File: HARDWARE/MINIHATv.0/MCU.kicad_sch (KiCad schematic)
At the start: 0 parts

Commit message: Merge branch 'main' into display-basic-implementation
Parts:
- added U2: STM32H747IGTx, Package_QFP:LQFP-176_24x24mm_P0.5mm, symbol MCU_ST_STM32H7:STM32H747IGTx
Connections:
- new net: U2.100 (VSS), U2.112 (VSS), U2.119 (VSS), U2.12 (VSS), U2.134 (VSS), U2.137 (VSS), U2.151 (VSS), U2.159 (VSS), U2.173 (VSS), U2.24 (VSS), U2.45 (VSS), U2.47 (VSS), U2.6 (VSS), U2.64 (VSS), U2.70 (VSS), U2.81 (VSS), U2.83 (VSS), U2.93 (VSS)
- new net: U2.105 (VSSDSI), U2.109 (VSSDSI)

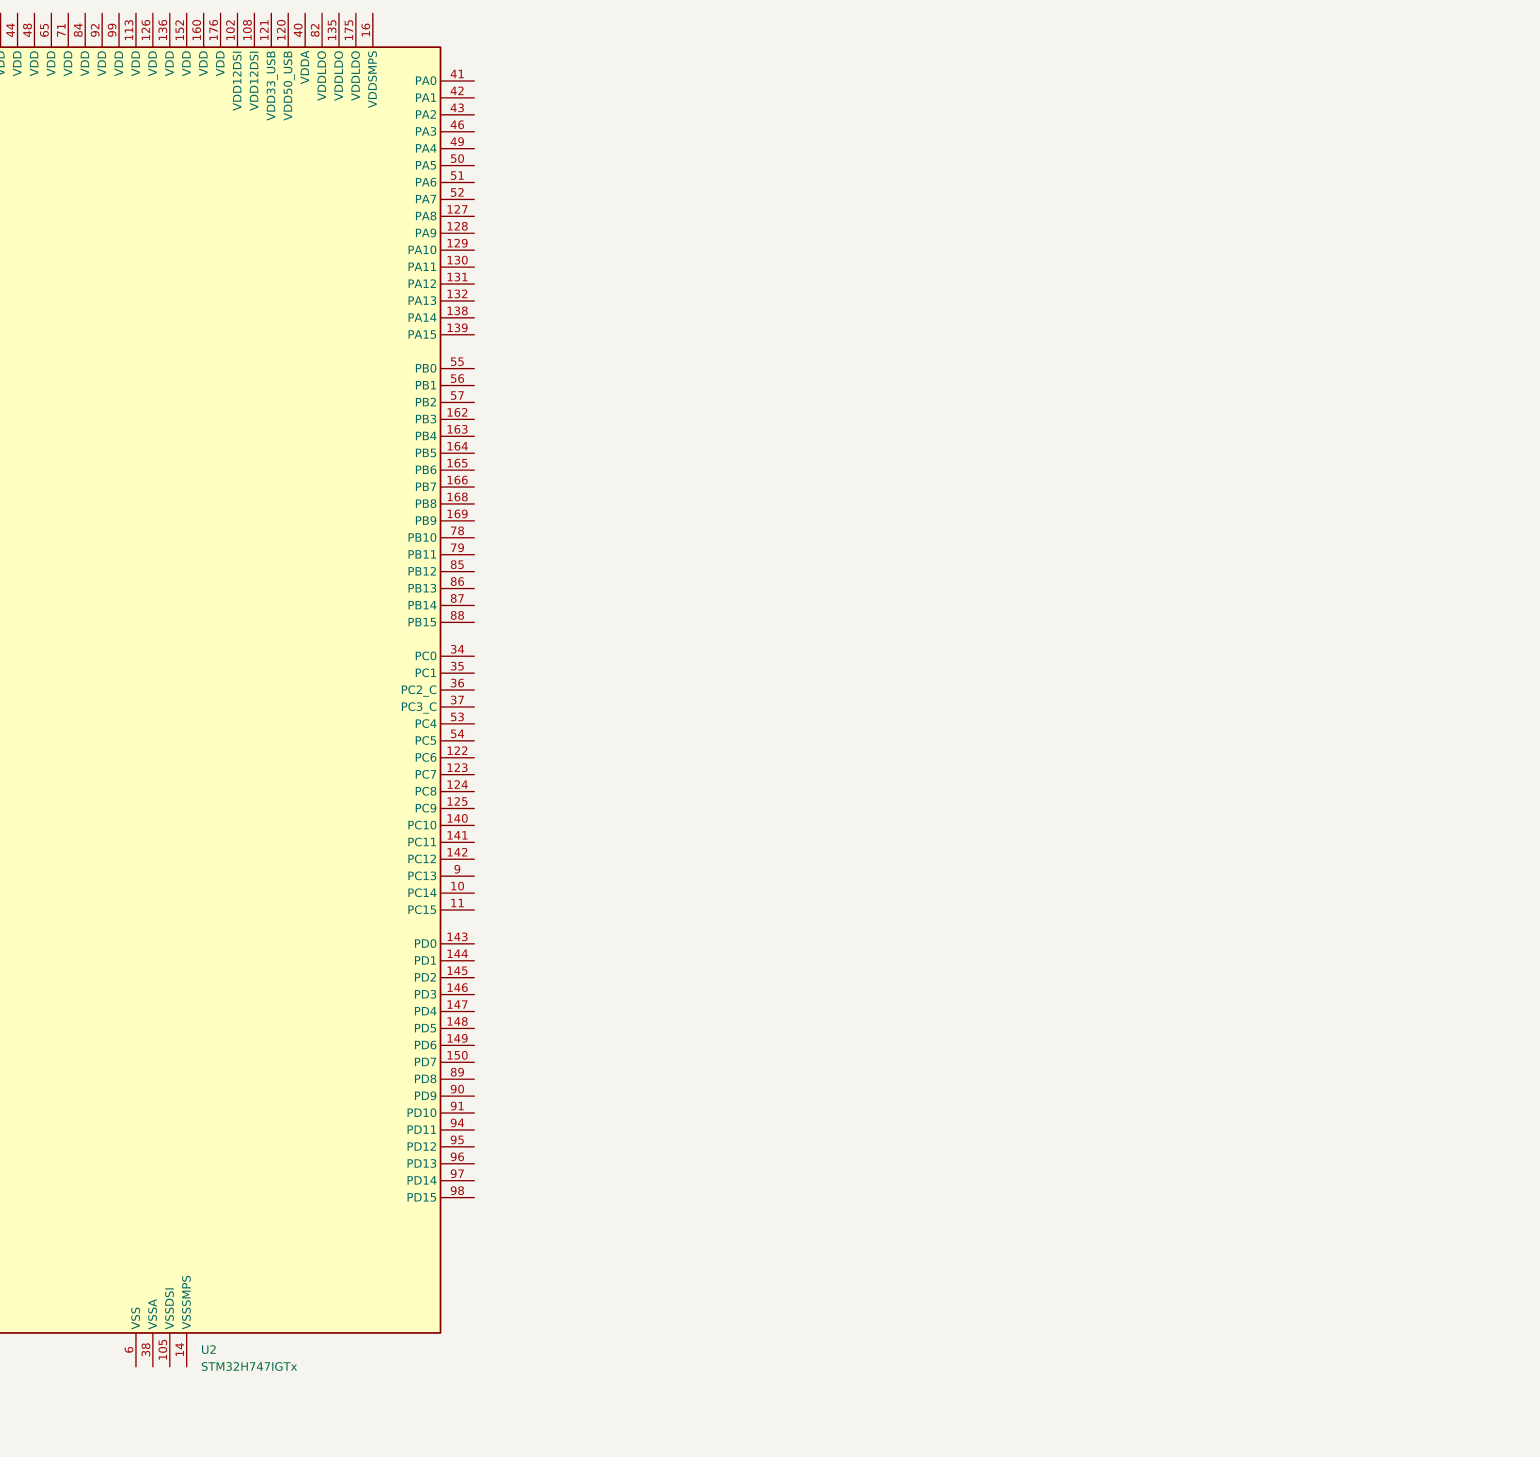
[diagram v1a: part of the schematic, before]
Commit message: added schematics for sd card and qspi flash
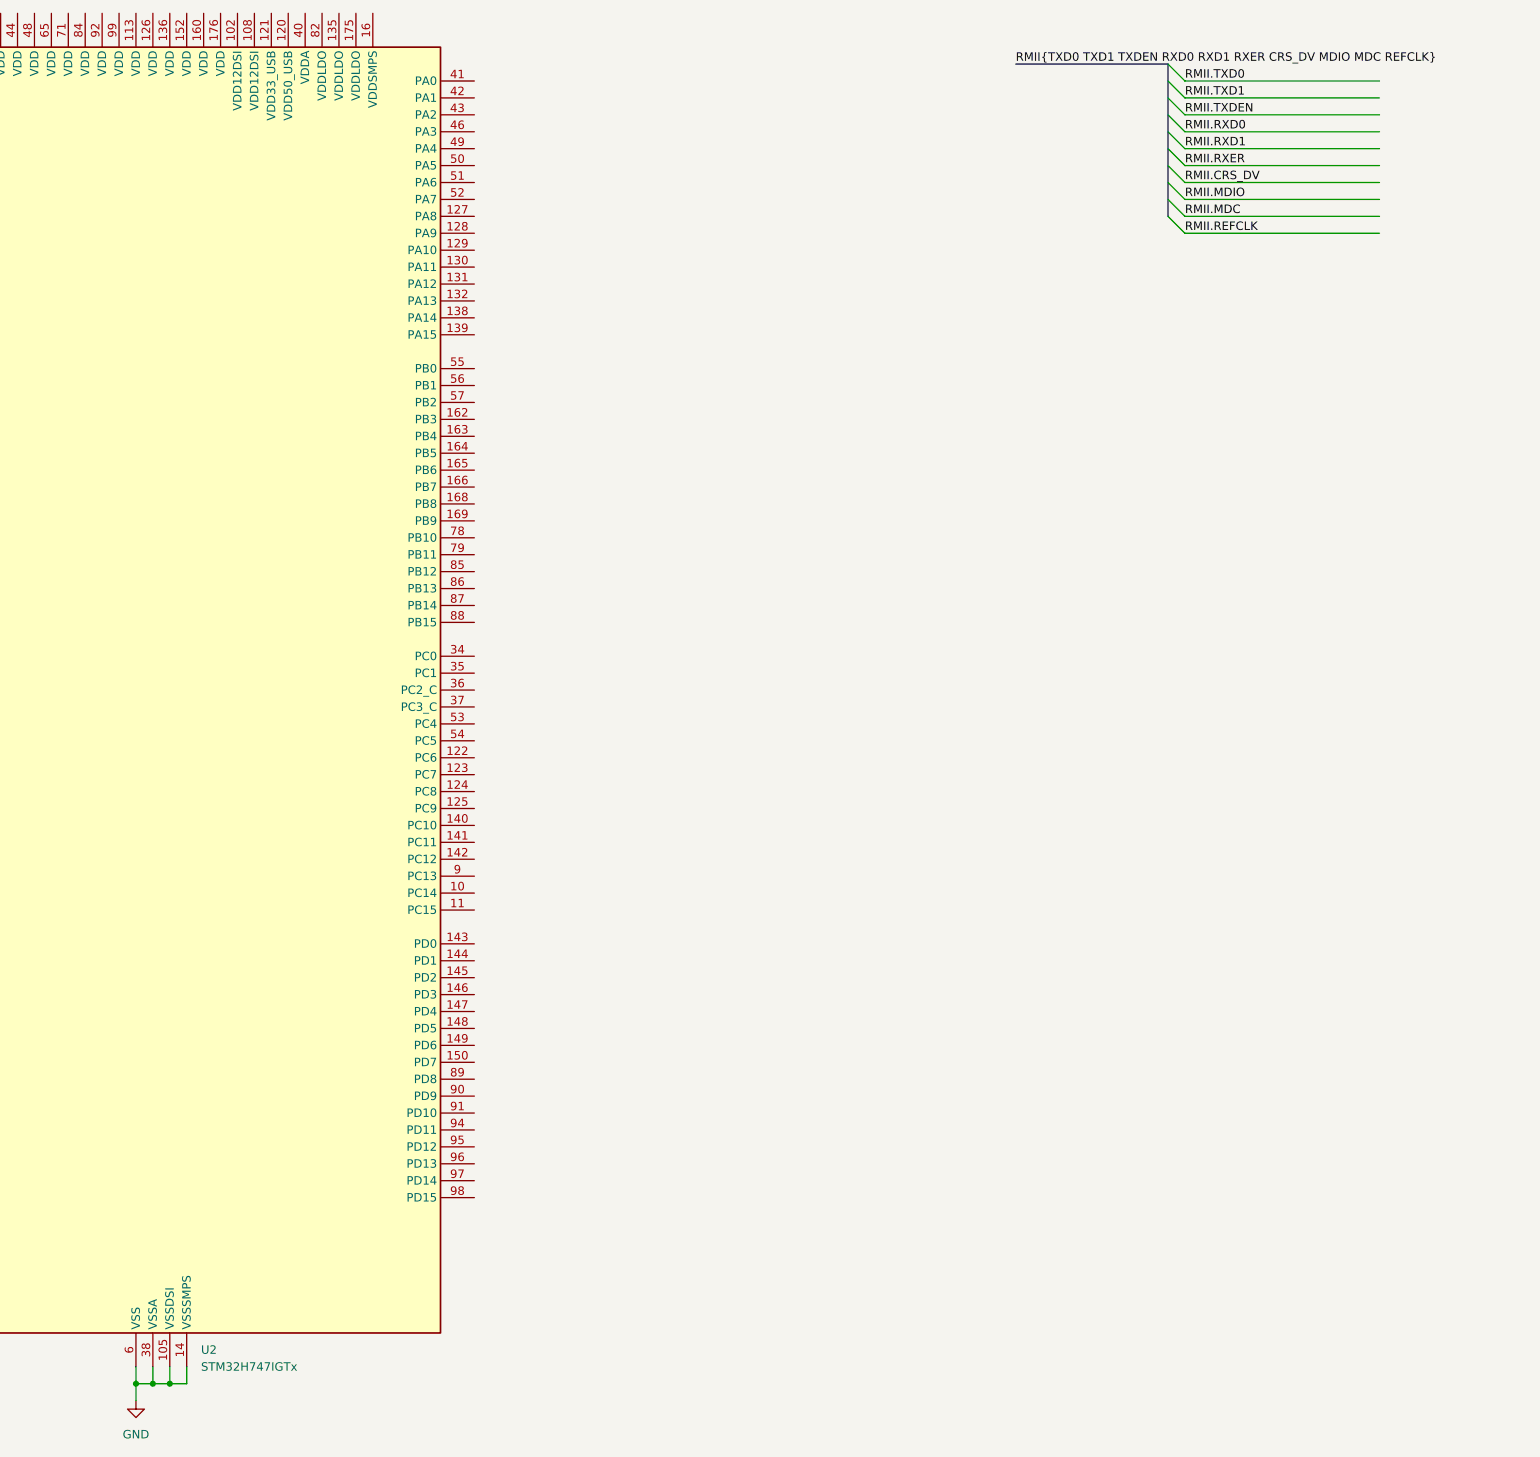
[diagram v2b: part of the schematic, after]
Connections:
- net GND: now reaches U2.100 (VSS), U2.112 (VSS), U2.119 (VSS), U2.12 (VSS), U2.134 (VSS), U2.137 (VSS), U2.151 (VSS), U2.159 (VSS), U2.173 (VSS), U2.24 (VSS), U2.45 (VSS), U2.47 (VSS), U2.6 (VSS), U2.64 (VSS), U2.70 (VSS), U2.81 (VSS), U2.83 (VSS), U2.93 (VSS)
- net GND: now also U2.105 (VSSDSI), U2.109 (VSSDSI), U2.14 (VSSSMPS), U2.38 (VSSA)

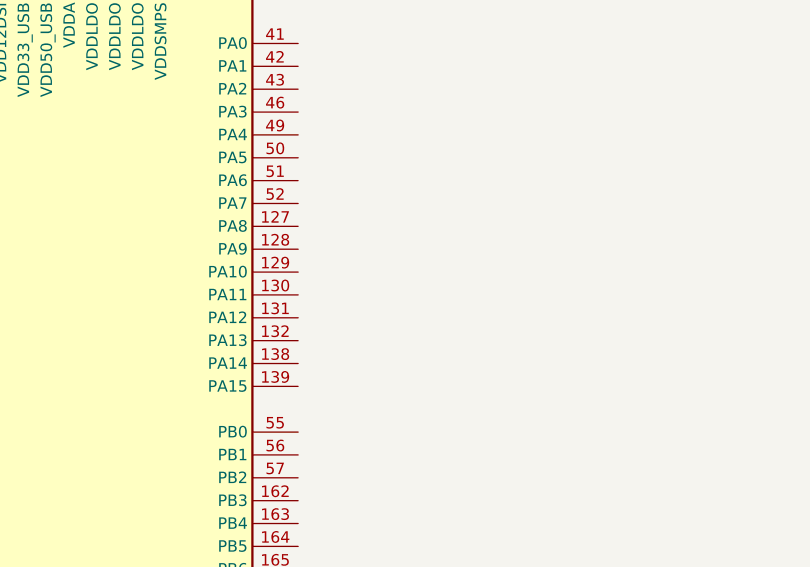
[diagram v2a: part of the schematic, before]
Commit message: added usb
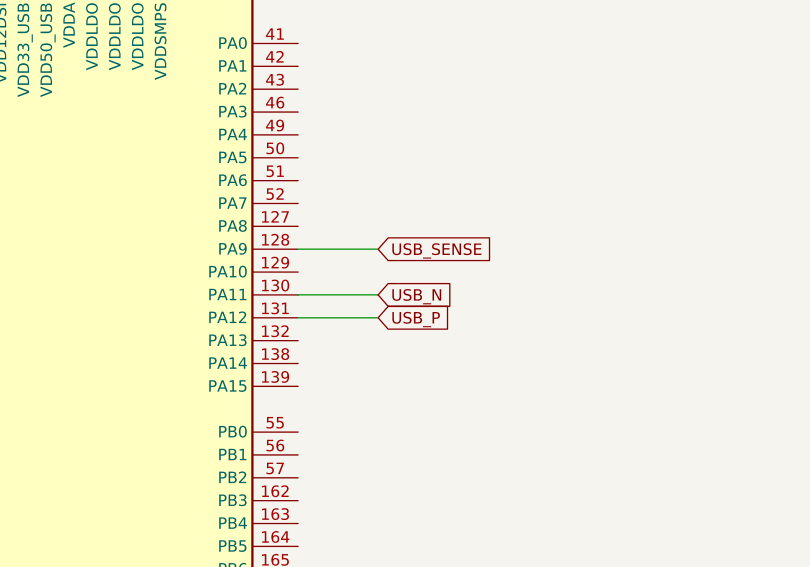
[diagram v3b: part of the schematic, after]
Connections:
- net USB_SENSE: now reaches U2.128 (PA9)
- net USB_N: now reaches U2.130 (PA11)
- net USB_P: now reaches U2.131 (PA12)
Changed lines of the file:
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@@
+	(wire
+		(pts
+			(xy 252.73 69.85) (xy 261.62 69.85)
+		)
+		(stroke
+			(width 0)
+			(type default)
+		)
+	)
 	(wire
 		(pts
@@
 	(wire
 		(pts
+			(xy 252.73 77.47) (xy 261.62 77.47)
+		)
+		(stroke
+			(width 0)
+			(type default)
+		)
+	)
+	(wire
+		(pts
 			(xy 201.93 245.11) (xy 201.93 242.57)
 		)
@@
 		(pts
 			(xy 359.41 57.15) (xy 388.62 57.15)
+		)
+		(stroke
+			(width 0)
+			(type default)
+		)
+	)
+	(wire
+		(pts
+			(xy 252.73 74.93) (xy 261.62 74.93)
 		)
 		(stroke
@@
 		)
 	)
+	(global_label "USB_SENSE"
+		(shape input)
+		(at 261.62 69.85 0)
+		(fields_autoplaced yes)
+		(effects
+			(font
+				(size 1.27 1.27)
+			)
+			(justify left)
+		)
+		(property "Intersheetrefs" "${INTERSHEET_REFS}"
+			(at 275.4303 69.85 0)
+			(hide yes)
+			(show_name no)
+			(do_not_autoplace no)
+			(effects
+				(font
+					(size 1.27 1.27)
+				)
+				(justify left)
+			)
+		)
+	)
+	(global_label "USB_N"
+		(shape input)
+		(at 261.62 74.93 0)
+		(fields_autoplaced yes)
+		(effects
+			(font
+				(size 1.27 1.27)
+			)
+			(justify left)
+		)
+		(property "Intersheetrefs" "${INTERSHEET_REFS}"
+			(at 270.7133 74.93 0)
+			(hide yes)
+			(show_name no)
+			(do_not_autoplace no)
+			(effects
+				(font
+					(size 1.27 1.27)
+				)
+				(justify left)
+			)
+		)
+	)
+	(global_label "USB_P"
+		(shape input)
+		(at 261.62 77.47 0)
+		(fields_autoplaced yes)
+		(effects
+			(font
+				(size 1.27 1.27)
+			)
+			(justify left)
+		)
+		(property "Intersheetrefs" "${INTERSHEET_REFS}"
+			(at 270.6528 77.47 0)
+			(hide yes)
+			(show_name no)
+			(do_not_autoplace no)
+			(effects
+				(font
+					(size 1.27 1.27)
+				)
+				(justify left)
+			)
+		)
+	)

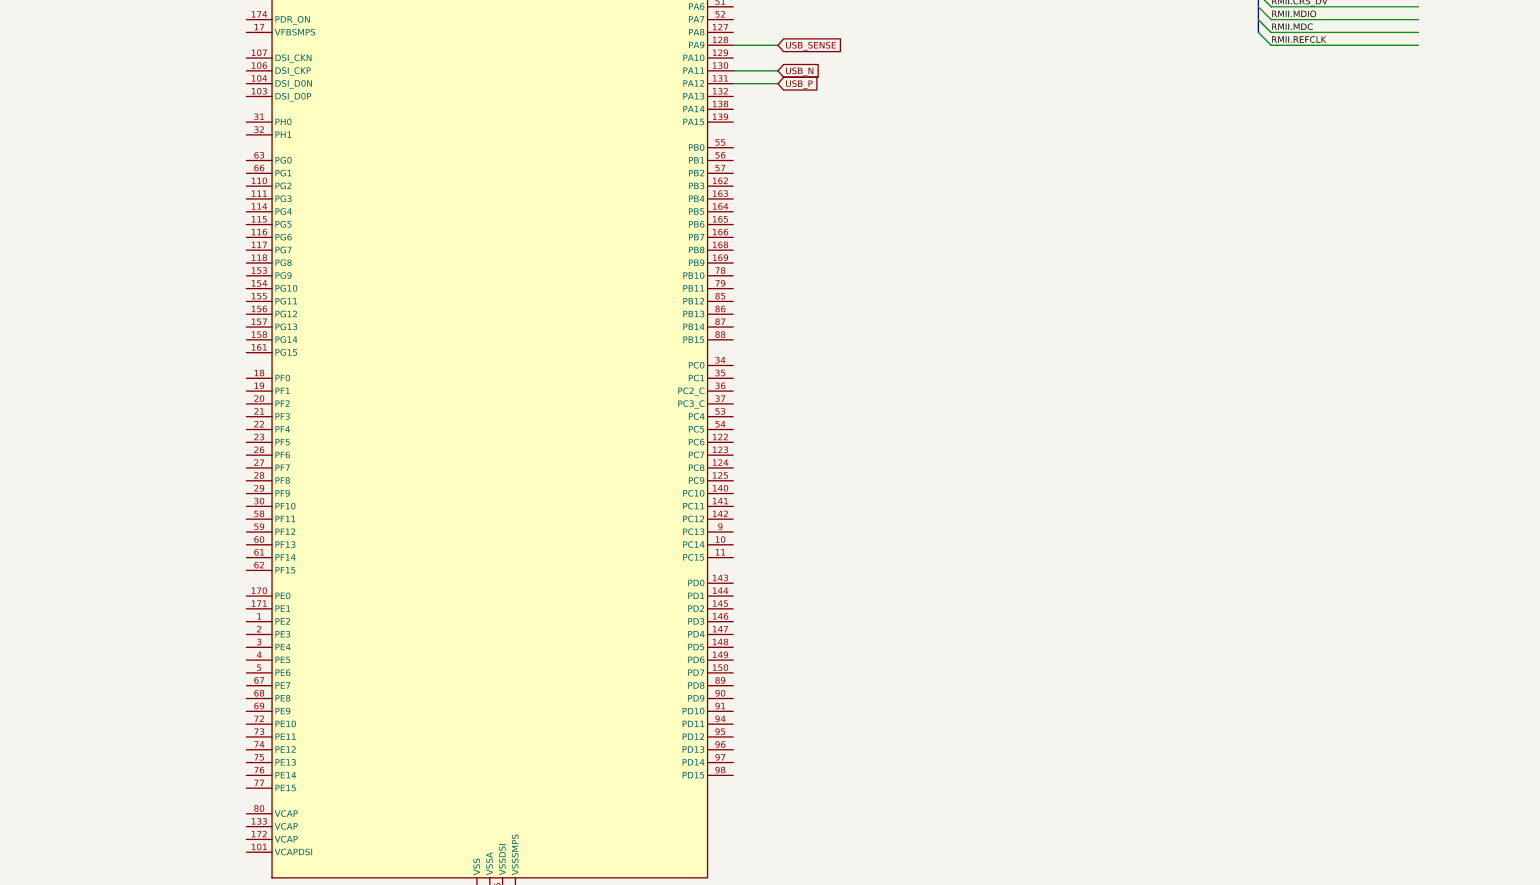
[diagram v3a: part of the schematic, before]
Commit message: added termination resistors , fixed data bus texts
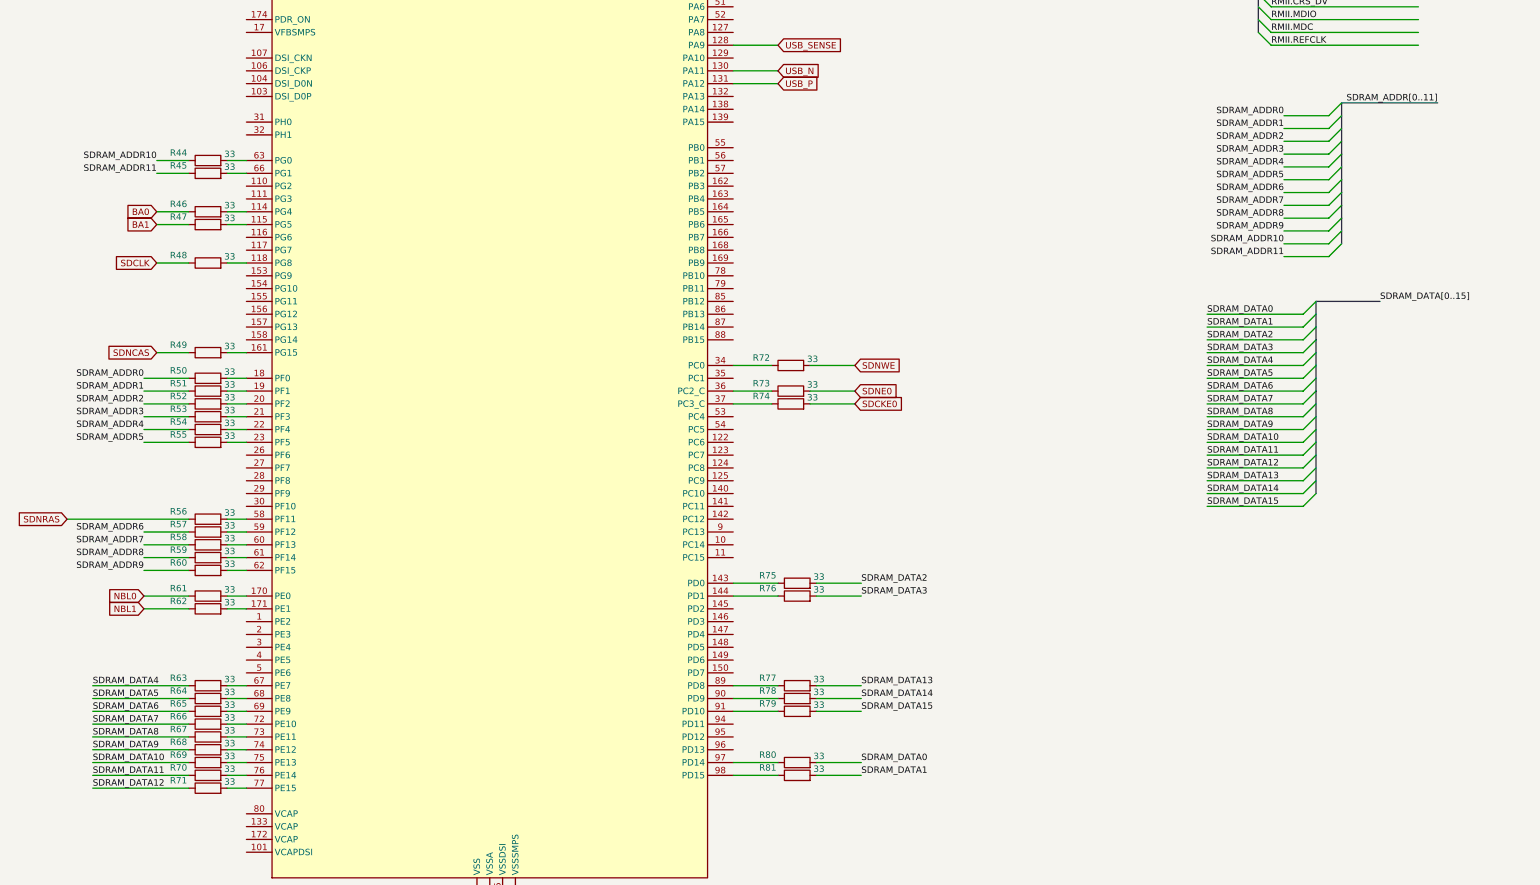
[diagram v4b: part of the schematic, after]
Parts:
- added R44, R45, R46, R47, R48, R49, R50, R51, R52, R53, R54, R55, R56, R57, R58, R59, R60, R61, R62, R63, R64, R65, R66, R67, R68, R69, R70, R71, R72, R73, R74, R75, R76, R77, R78, R79, R80, R81: 33, symbol Device:R
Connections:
- net at U2.114 (PG4): now also R46.2
- net at U2.115 (PG5): now also R47.2
- net at U2.118 (PG8): now also R48.2
- net at U2.143 (PD0): now also R75.1
- net at U2.144 (PD1): now also R76.1
- net at U2.161 (PG15): now also R49.2
- net at U2.170 (PE0): now also R61.2
- net at U2.171 (PE1): now also R62.2
- net at U2.18 (PF0): now also R50.2
- net at U2.19 (PF1): now also R51.2
- net at U2.20 (PF2): now also R52.2
- net at U2.21 (PF3): now also R53.2
- net at U2.22 (PF4): now also R54.2
- net at U2.23 (PF5): now also R55.2
- net at U2.34 (PC0): now also R72.1
- net at U2.36 (PC2_C): now also R73.1
- net at U2.37 (PC3_C): now also R74.1
- net at U2.58 (PF11): now also R56.2
- net at U2.59 (PF12): now also R57.2
- net at U2.60 (PF13): now also R58.2
- net at U2.61 (PF14): now also R59.2
- net at U2.62 (PF15): now also R60.2
- net at U2.63 (PG0): now also R44.2
- net at U2.66 (PG1): now also R45.2
- net at U2.67 (PE7): now also R63.2
- net at U2.68 (PE8): now also R64.2
- net at U2.69 (PE9): now also R65.2
- net at U2.72 (PE10): now also R66.2
- net at U2.73 (PE11): now also R67.2
- net at U2.74 (PE12): now also R68.2
- net at U2.75 (PE13): now also R69.2
- net at U2.76 (PE14): now also R70.2
- net at U2.77 (PE15): now also R71.2
- net at U2.89 (PD8): now also R77.1
- net at U2.90 (PD9): now also R78.1
- net at U2.91 (PD10): now also R79.1
- net at U2.97 (PD14): now also R80.1
- net at U2.98 (PD15): now also R81.1
- new net BA0: R46.1
- new net BA1: R47.1
- new net NBL0: R61.1
- new net NBL1: R62.1
- new net SDCKE0: R74.2
- new net SDCLK: R48.1
- new net SDNCAS: R49.1
- new net SDNE0: R73.2
- new net SDNRAS: R56.1
- new net SDNWE: R72.2
- new net SDRAM_ADDR0: R50.1
- new net SDRAM_ADDR1: R51.1
- new net SDRAM_ADDR10: R44.1
- new net SDRAM_ADDR11: R45.1
- new net SDRAM_ADDR2: R52.1
- new net SDRAM_ADDR3: R53.1
- new net SDRAM_ADDR4: R54.1
- new net SDRAM_ADDR5: R55.1
- new net SDRAM_ADDR6: R57.1
- new net SDRAM_ADDR7: R58.1
- new net SDRAM_ADDR8: R59.1
- new net SDRAM_ADDR9: R60.1
- new net SDRAM_DATA0: R80.2
- new net SDRAM_DATA1: R81.2
- new net SDRAM_DATA10: R69.1
- new net SDRAM_DATA11: R70.1
- new net SDRAM_DATA12: R71.1
- new net SDRAM_DATA13: R77.2
- new net SDRAM_DATA14: R78.2
- new net SDRAM_DATA15: R79.2
- new net SDRAM_DATA2: R75.2
- new net SDRAM_DATA3: R76.2
- new net SDRAM_DATA4: R63.1
- new net SDRAM_DATA5: R64.1
- new net SDRAM_DATA6: R65.1
- new net SDRAM_DATA7: R66.1
- new net SDRAM_DATA8: R67.1
- new net SDRAM_DATA9: R68.1

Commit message: added normal buses
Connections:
- net SDCKE0 renamed SDCKEO
- net SDNE0 renamed SDNEO

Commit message: fixed ltdc and other peripheral pin conflicts
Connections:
- net RMII.CRS_DV: now also U2.52 (PA7)
- net RMII.MDC: now also U2.35 (PC1)
- net RMII.MDIO: now also U2.43 (PA2)
- net RMII.REFCLK: now also U2.42 (PA1)
- net RMII.RXD0: now also U2.53 (PC4)
- net RMII.RXD1: now also U2.54 (PC5)
- net RMII.TXD0: now also U2.156 (PG12)
- net RMII.TXD1: now also U2.157 (PG13)
- net RMII.TXDEN: now also U2.155 (PG11)
- net SDIO.DAT0: now reaches U2.124 (PC8)
- net SDIO.DAT1: now reaches U2.125 (PC9)
- net SDIO.DAT2: now reaches U2.140 (PC10)
- net SDIO.DAT3: now reaches U2.141 (PC11)
- net SDIO.CLK: now reaches U2.142 (PC12)
- net SDIO.CMD: now reaches U2.145 (PD2)
